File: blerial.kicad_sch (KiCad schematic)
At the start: 9 parts, among them J1 Header, SW1 Power Switch, U1 JDY-23-Module, U2 MIC5504-3.3YM5

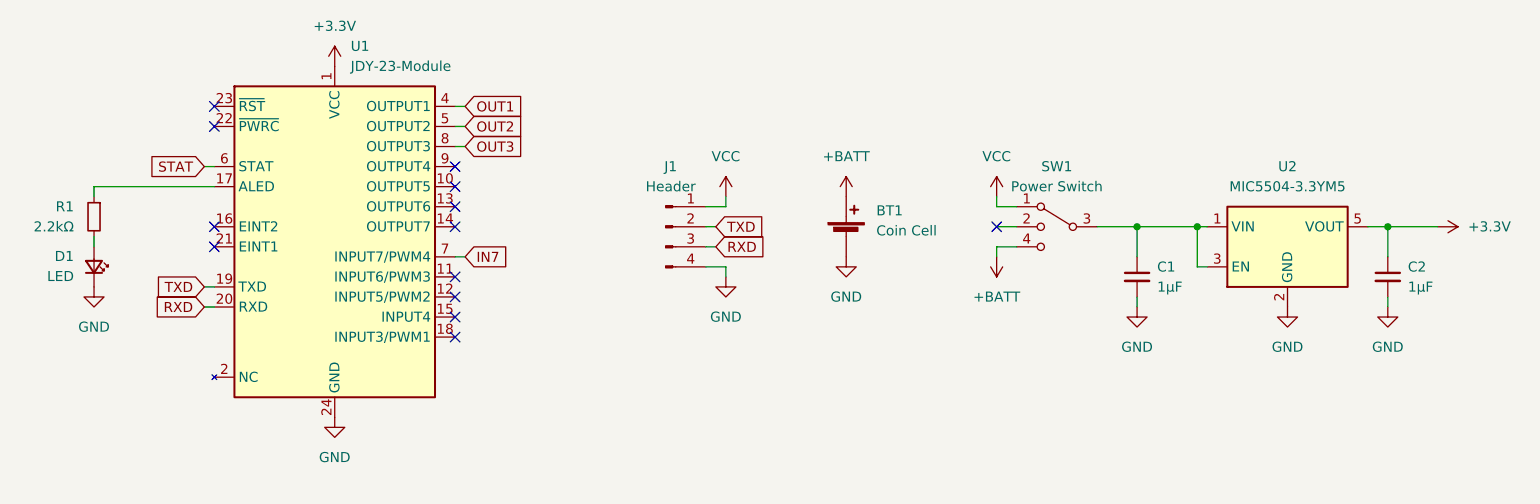
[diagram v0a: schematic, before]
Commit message: edit to switch between bat / 3.3 regulator
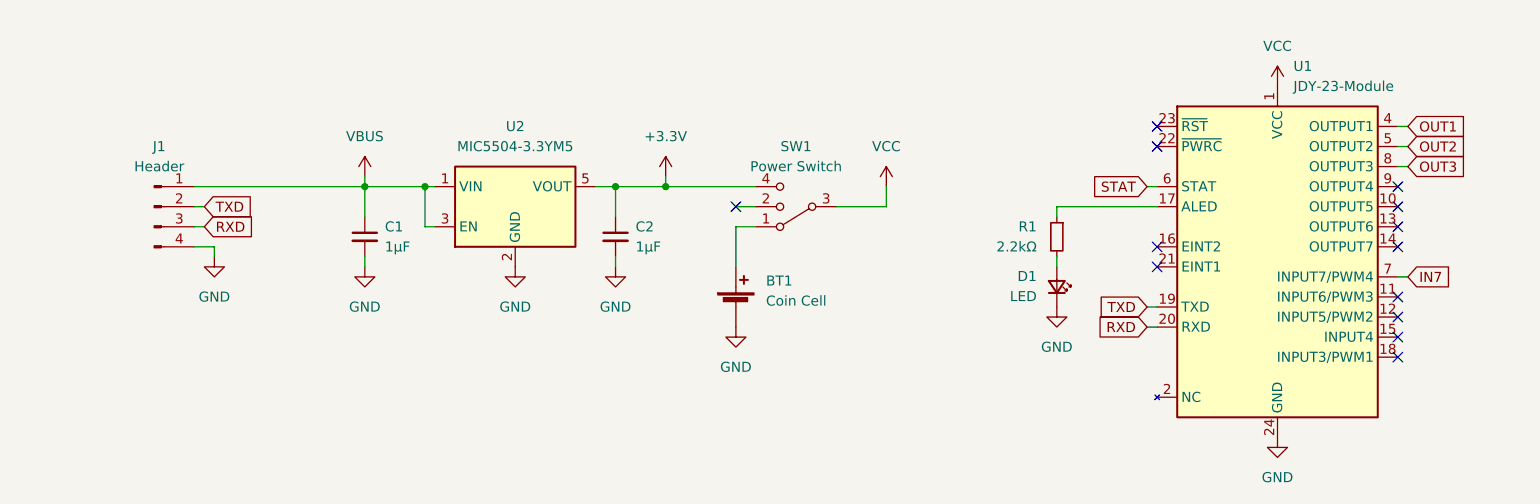
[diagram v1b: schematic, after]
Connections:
- net +3V3: now also SW1.4; no longer U1.1 (VCC)
- net VCC: now also SW1.3, U1.1 (VCC); no longer J1.1 (Pin_1), SW1.1
- net VBUS: now reaches C1.1, U2.1 (VIN), U2.3 (EN)
- net VBUS: now also J1.1 (Pin_1); no longer SW1.3
- net +BATT: no longer names the net of BT1.1 (+)
- net +BATT: now also SW1.1; no longer SW1.4
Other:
- moved on the sheet: BT1, C1, C2, D1, J1, R1, SW1, U1, U2

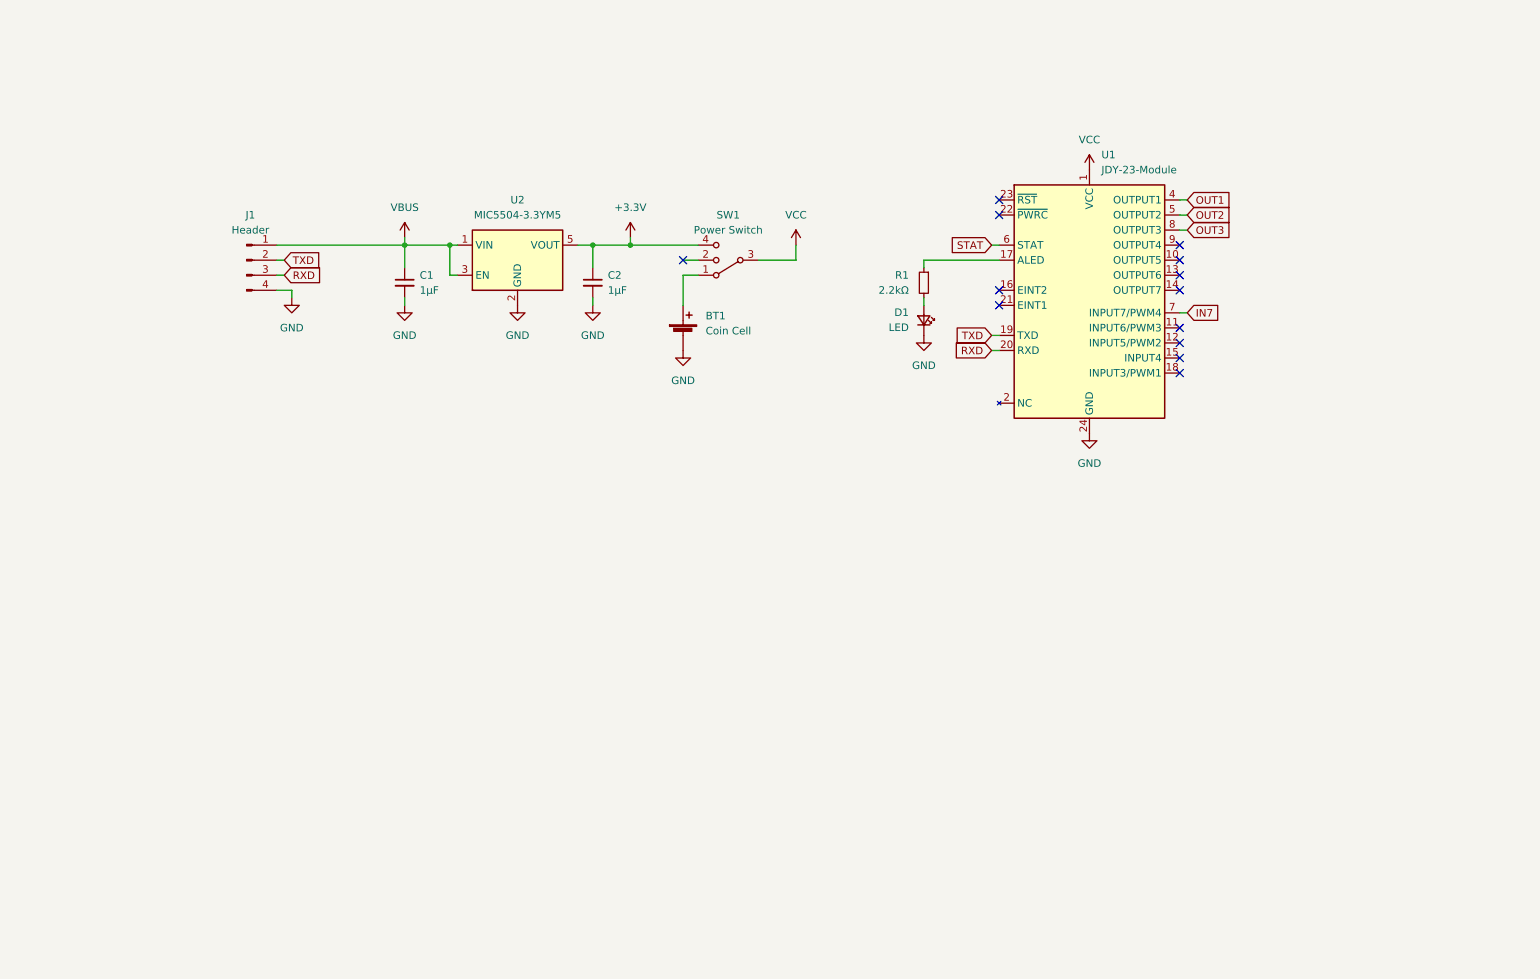
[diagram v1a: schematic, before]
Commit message: rerouted for HM-19, but not very tidy
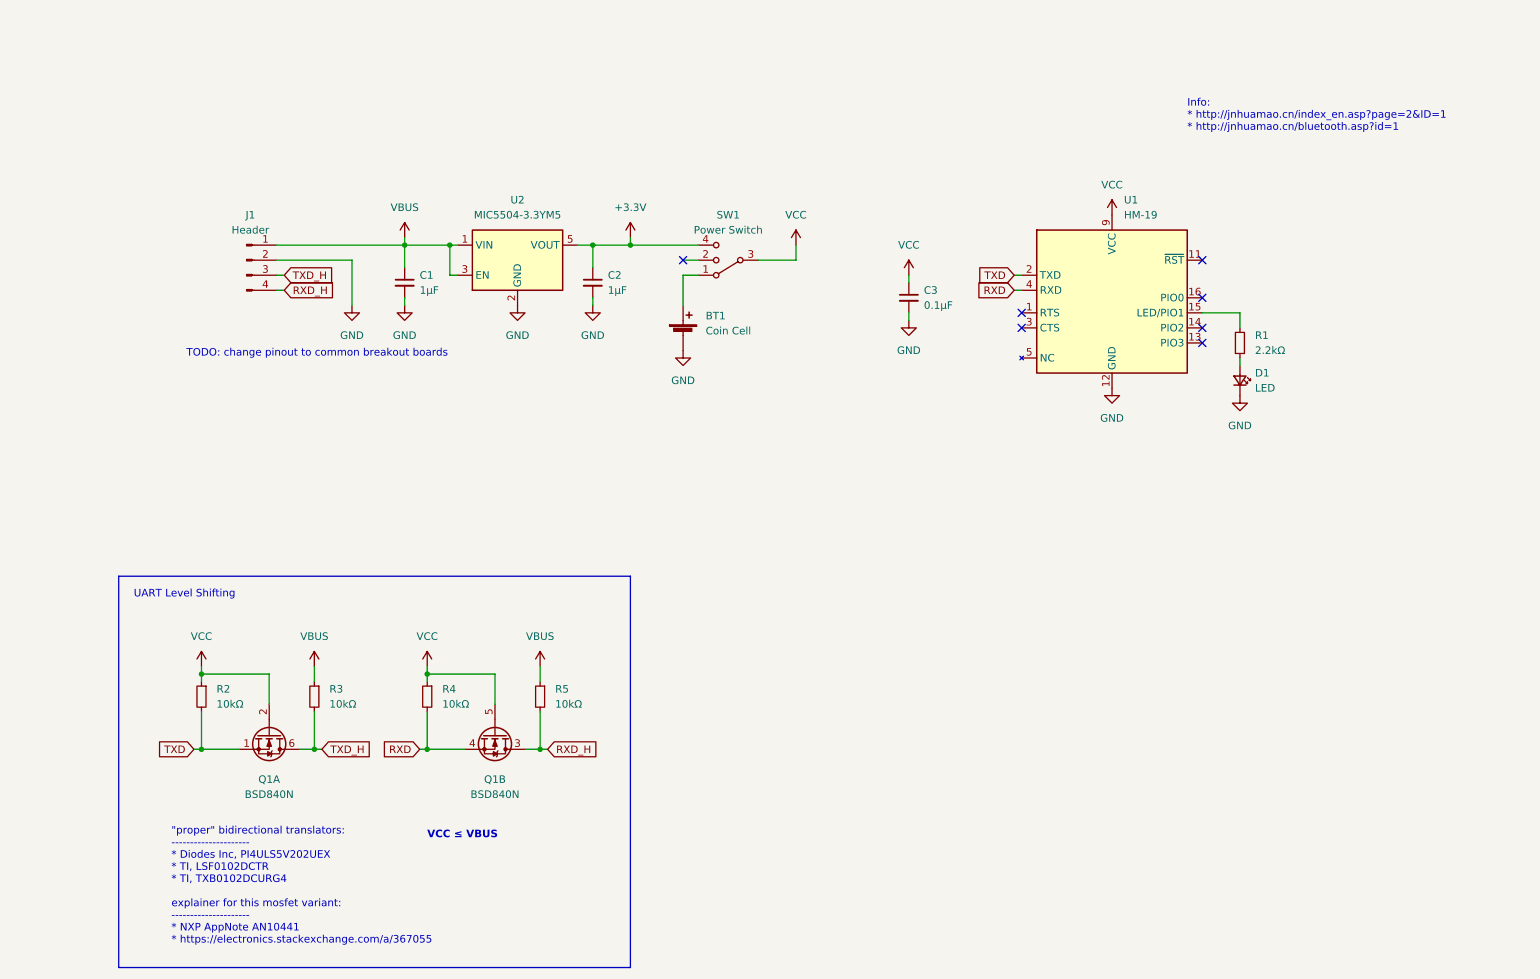
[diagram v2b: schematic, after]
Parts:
- removed U1: JDY-23-Module, jdy:JDY-23, symbol jdy:JDY-23-Module
- added C3: 0.1µF, Capacitor_SMD:C_0805_2012Metric, symbol Device:C_Small
- added Q1: BSD840N, Package_TO_SOT_SMD:SOT-363_SC-70-6, symbol Transistor_FET:FDG1024NZ
- added R2, R3, R4, R5: 10kΩ, Resistor_SMD:R_0805_2012Metric, symbol Device:R_Small
- added U1: HM-19, blerial:HM-19, symbol blerial:HM-19
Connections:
- net GND: now also J1.2 (Pin_2), C3.2, U1.12 (GND); no longer J1.4 (Pin_4)
- net RXD: now also Q1.4 (S), R4.2, U1.4 (RXD); no longer J1.3 (Pin_3)
- net TXD: now also Q1.1 (S), R2.2, U1.2 (TXD); no longer J1.2 (Pin_2)
- net VBUS: now also R3.1, R5.1
- net VCC: now also C3.1, Q1.2 (G), Q1.5 (G), R2.1, R4.1, U1.9 (VCC)
- net at R1.2: now also U1.15 (LED/PIO1); no longer D1.2 (A)
- net at R1.1: now also D1.2 (A)
- new net: U1.10 (NC), U1.5 (NC), U1.6 (NC), U1.7 (NC), U1.8 (NC)
- new net RXD_H: J1.4 (Pin_4), Q1.3 (D), R5.2
- new net TXD_H: J1.3 (Pin_3), Q1.6 (D), R3.2
- no-connect marks 13 -> 7
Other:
- note added: ""proper" bidirectional translators: --------------------- * Diodes Inc, PI4ULS5V202UEX * TI, LSF0102DCTR * TI, TXB0102DCURG4 explainer for this mosfet variant: --------------------- * NXP AppNote AN10441 * https://electronics.stackexchange.com/a/367055"
- note added: "Info: * http://jnhuamao.cn/index_en.asp?page=2&ID=1 * http://jnhuamao.cn/bluetooth.asp?id=1"
- note added: "TODO: change pinout to common breakout boards"
- note added: "UART Level Shifting"
- note added: "VCC ≤ VBUS"
- moved on the sheet: D1, R1

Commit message: finished redesign with 200µm net class, rotated battery
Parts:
- removed SW1: Power Switch, Button_Switch_SMD:SW_SP3T_PCM13, symbol Switch:SW_SP3T
- added C4: 1µF, Capacitor_SMD:C_0805_2012Metric, symbol Device:C_Small
- added D2, D3: D_Small, Diode_SMD:D_SOD-123, symbol Device:D_Small
- added SW1: ON/OFF, Button_Switch_SMD:SW_SPDT_PCM12, symbol Switch:SW_SPDT
- Q1: value BSD840N -> FDG1024NZ
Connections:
- net +3V3: now also D2.2 (A)
- net GND: now also J1.3 (Pin_3), C4.2; no longer J1.2 (Pin_2)
- net RXD_H: now also J1.1 (Pin_1); no longer J1.4 (Pin_4)
- net TXD_H: now also J1.2 (Pin_2); no longer J1.3 (Pin_3)
- net VBUS: now also J1.4 (Pin_4); no longer J1.1 (Pin_1)
- net VCC: now also C4.1, SW1.3 (C)
- net at BT1.1 (+): now also D3.2 (A)
- new net: D2.1 (K), D3.1 (K), SW1.2 (B)
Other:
- note removed: "TODO: change pinout to common breakout boards"
- moved on the sheet: BT1, C1, C2, C3, J1, U2

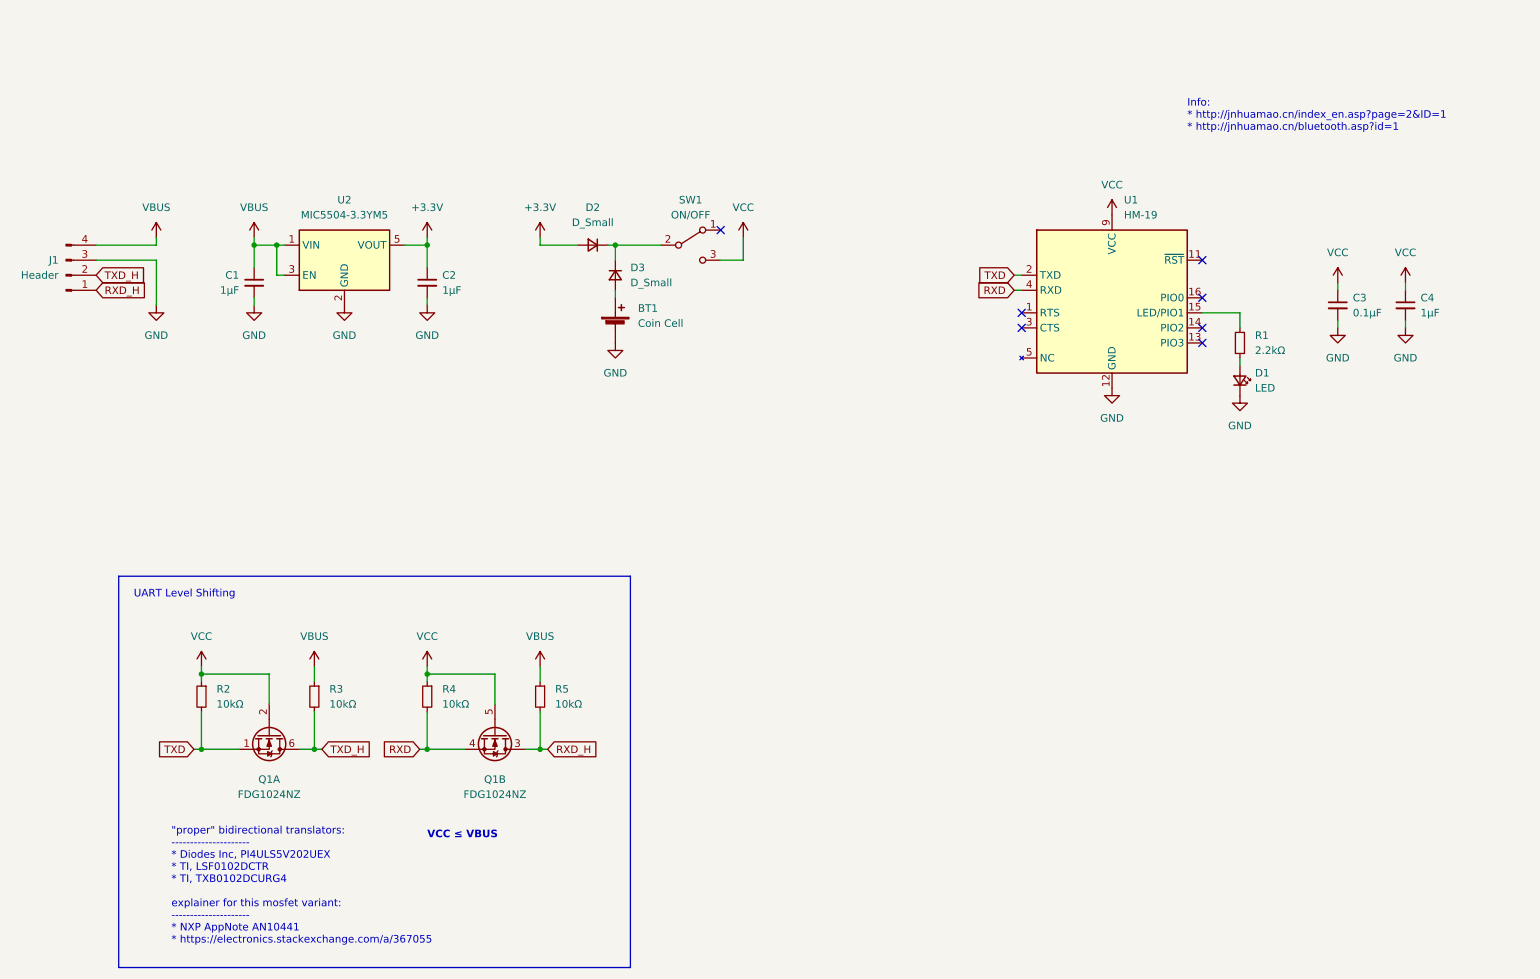
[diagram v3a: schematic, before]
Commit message: small tweaks, correct diode and mosfet pns
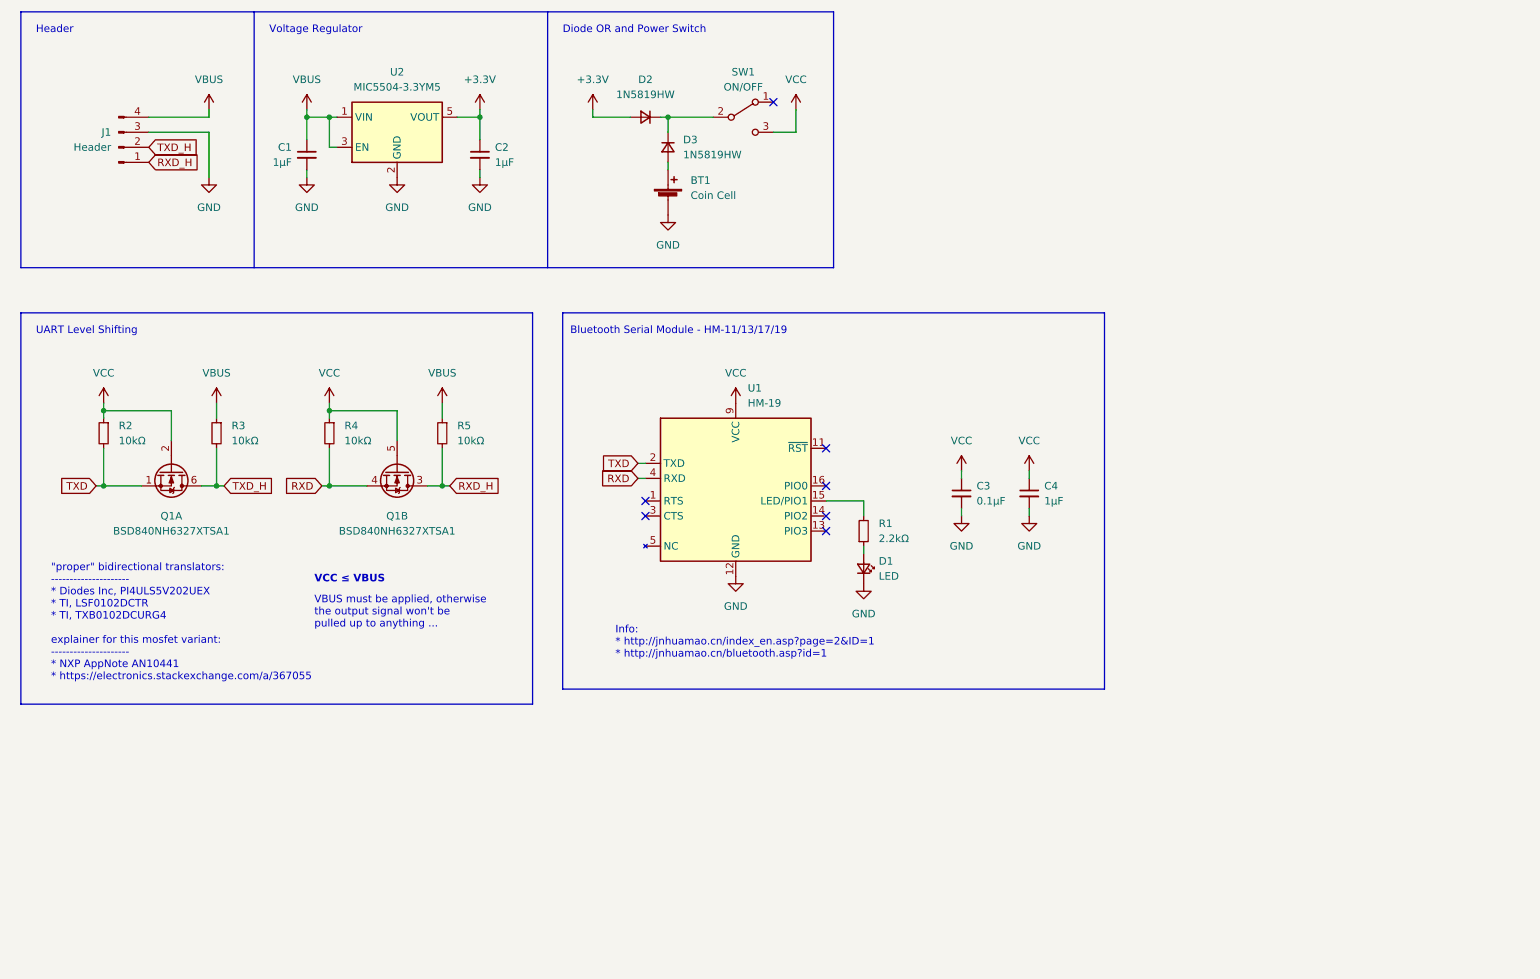
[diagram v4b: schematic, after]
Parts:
- D2, D3: value D_Small -> 1N5819HW
- Q1: value FDG1024NZ -> BSD840NH6327XTSA1
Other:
- note added: "Bluetooth Serial Module - HM-11/13/17/19"
- note added: "Diode OR and Power Switch"
- note added: "Header"
- note added: "VBUS must be applied, otherwise the output signal won't be pulled up to anything ..."
- note added: "Voltage Regulator"
- company: (none) -> ansemjo
- title: (none) -> BLErial
- moved on the sheet: BT1, C1, C2, C3, C4, D1, D2, D3, J1, Q1A, Q1B, R1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
